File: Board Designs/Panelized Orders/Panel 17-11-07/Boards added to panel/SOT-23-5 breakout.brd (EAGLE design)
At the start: 33 x 17.7 mm, 8 parts

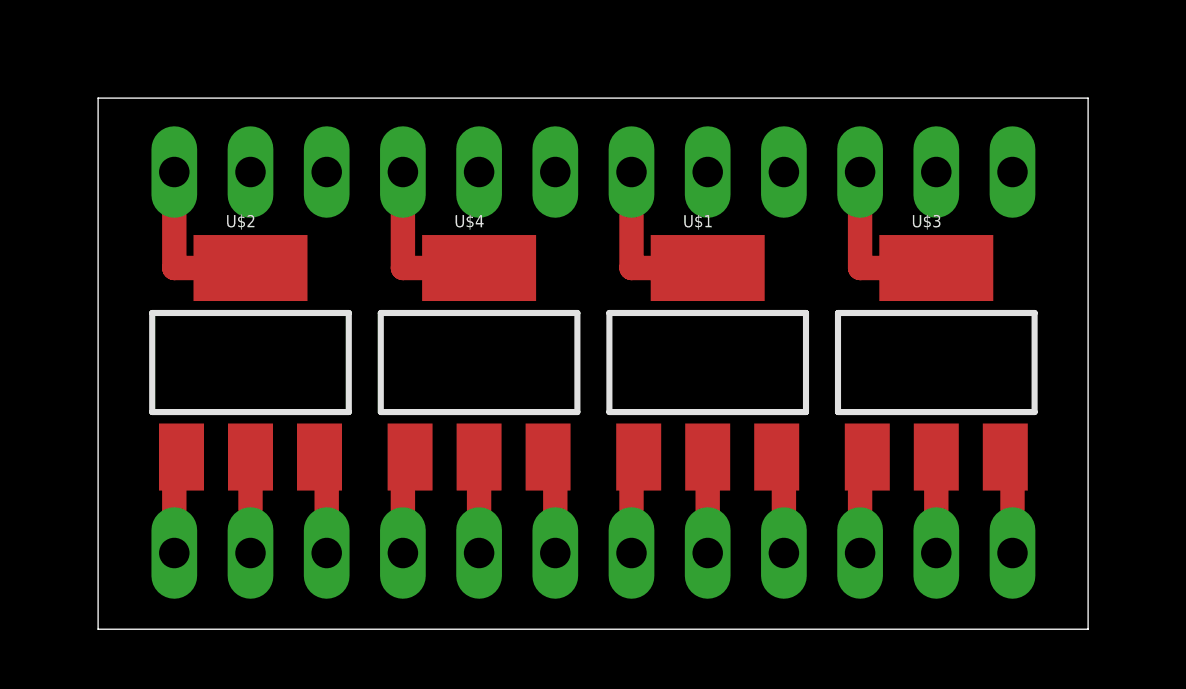
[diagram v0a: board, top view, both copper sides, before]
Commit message: Prep wiring harness board, silkscreen tweaks to front ecu, tweaks to breakout boards, finalized panels
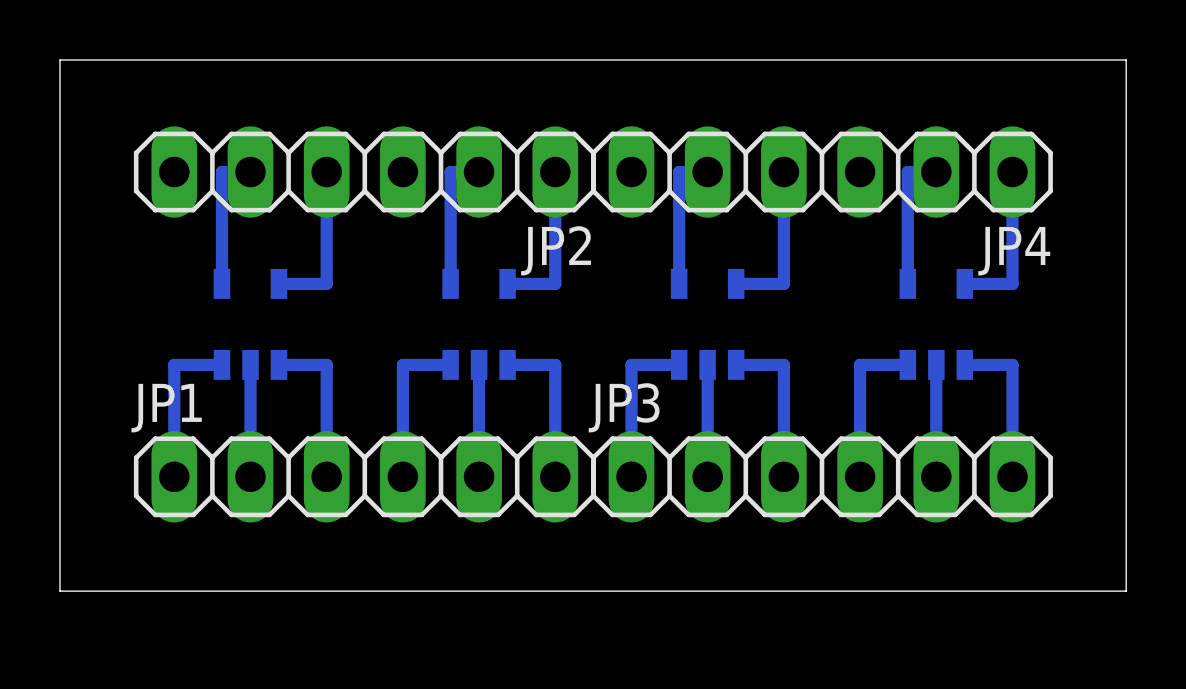
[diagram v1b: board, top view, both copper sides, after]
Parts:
- U$1, U$3: value SOT223 -> SN74LVC1G06; device HyTechDevices:SOT223 -> HyTechDevices:SOT-23-5
- U$2, U$4: value SOT223 -> SN74LVC1G07; device HyTechDevices:SOT223 -> HyTechDevices:SOT-23-5
- moved JP1 15.5 mm to (10.2, 3.81), flipped to the top
- moved JP3 15.5 mm to (25.4, 3.81), flipped to the top
- moved JP2 15.2 mm to (10.2, 14.0), flipped to the top
- moved JP4 15.2 mm to (25.4, 14.0), flipped to the top
- moved U$1 7.73 mm to (14.0, 8.89), flipped to the bottom, turned to 90 degrees
- moved U$4 7.73 mm to (21.6, 8.89), flipped to the bottom, turned to 90 degrees
- moved U$2 1.27 mm to (6.35, 8.89), flipped to the bottom, turned to 90 degrees
- moved U$3 1.27 mm to (29.2, 8.89), flipped to the bottom, turned to 90 degrees
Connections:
- removed net N$5 (its old number): JP1.3, U$3.1
- removed net N$6 (its old number): JP1.2, U$3.2
- removed net N$7 (its old number): JP1.1, U$3.3
- new net N$14: JP4.5, U$4.4
- new net N$15: JP3.6, U$3.1
- new net N$16: JP3.5, U$3.2
- new net N$17: JP3.4, U$3.3
- new net N$2: JP2.2, U$1.4
- new net N$3: JP2.4, U$2.5
- new net N$4: JP2.5, U$2.4
- net N$1: now also U$1.5; no longer U$1.4
- net N$10: now also JP1.1, U$2.3; no longer JP4.4, U$4.4
- net N$11: now also JP4.1, U$3.5; no longer JP3.6, U$2.1
- net N$12: now also JP4.2, U$3.4; no longer JP3.5, U$2.2
- net N$13: now also JP4.4, U$4.5; no longer JP3.4, U$2.3
- net N$8: now also JP1.3, U$2.1; no longer JP2.4, U$3.4
- net N$9: now also JP1.2, U$2.2; no longer JP4.1, U$2.4
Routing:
- net N$3: track 0.00 -> 5.32 mm
- net N$17: track 0.00 -> 5.32 mm
- net N$15: track 0.00 -> 5.32 mm
- net N$2: track 0.00 -> 4.68 mm
- net N$4: track 0.00 -> 4.68 mm
- net N$14: track 0.00 -> 4.68 mm
- net N$16: track 0.00 -> 3.73 mm
- net N$7 (its old number): track 3.44 -> 0.00 mm
- net N$5 (its old number): track 3.44 -> 0.00 mm
- net N$6 (its old number): track 3.20 -> 0.00 mm
- net N$9: track 5.74 -> 3.73 mm
- net N$5: track 3.44 -> 5.32 mm
- net N$7: track 3.44 -> 5.32 mm
- net N$11: track 3.44 -> 5.32 mm
- net N$18: track 3.44 -> 5.32 mm
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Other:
- board size 33 x 17.7 mm -> 35.5 x 17.7 mm
- board text removed: "HyTech Racing"
